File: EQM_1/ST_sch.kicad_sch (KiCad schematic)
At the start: 45 parts, among them J302 Screw_Terminal_01x05, U301 LM35-D, U302 TL082, U303 TL082, U304 LM4040DEX3-2.5+T, U305 TL082

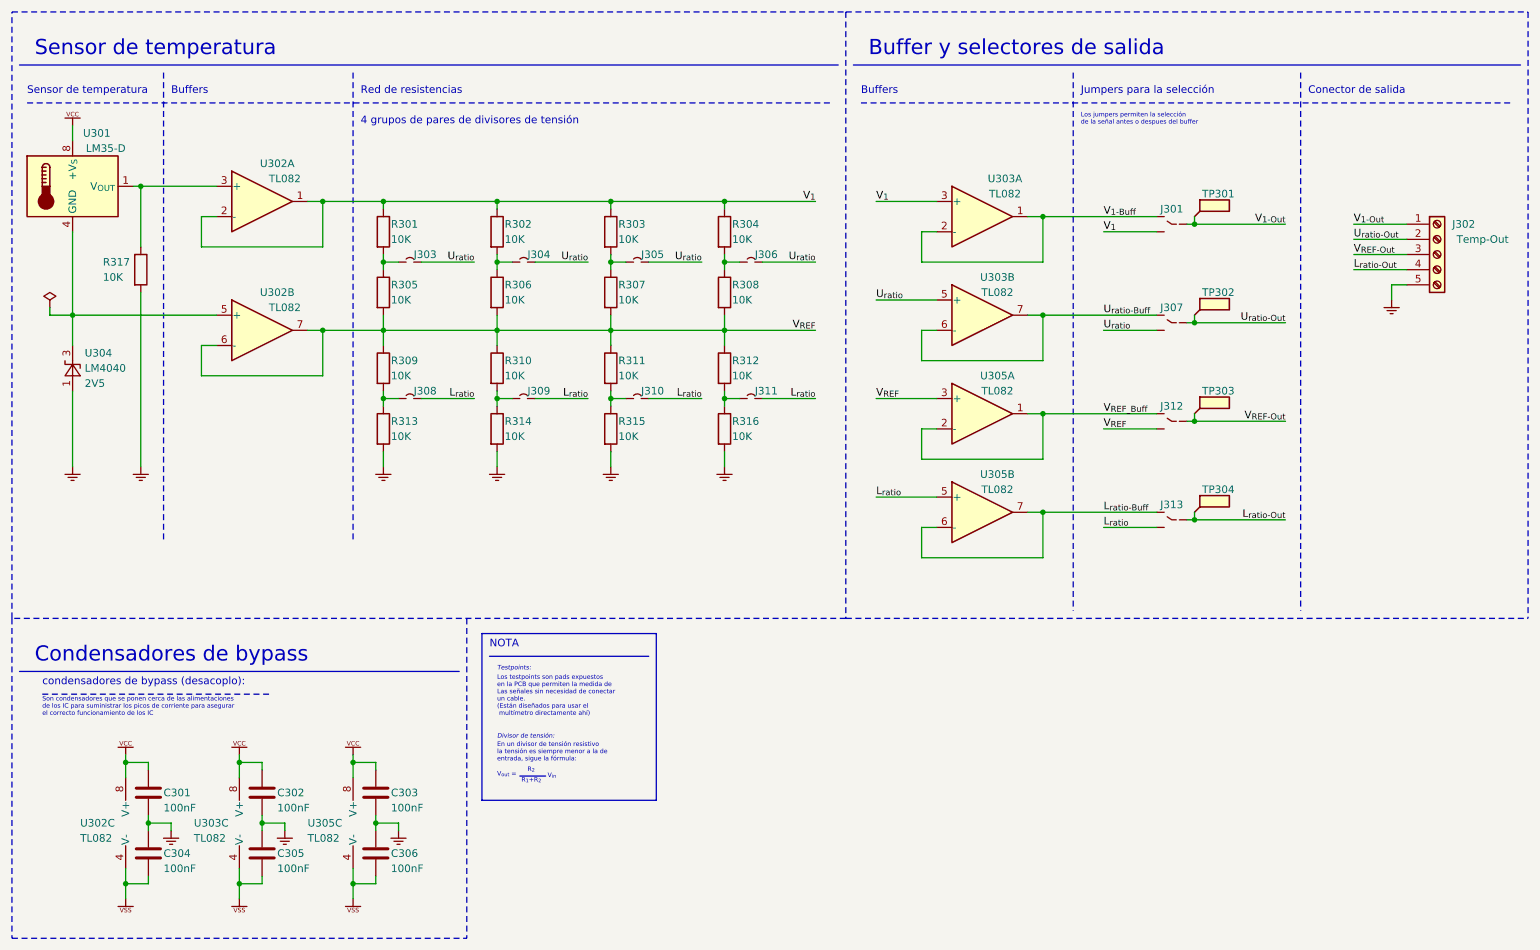
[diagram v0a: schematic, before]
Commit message: Esquema finalizado
El esquema está finalizado a falta de la asociación de footprints y la selección de valores para los pasivos
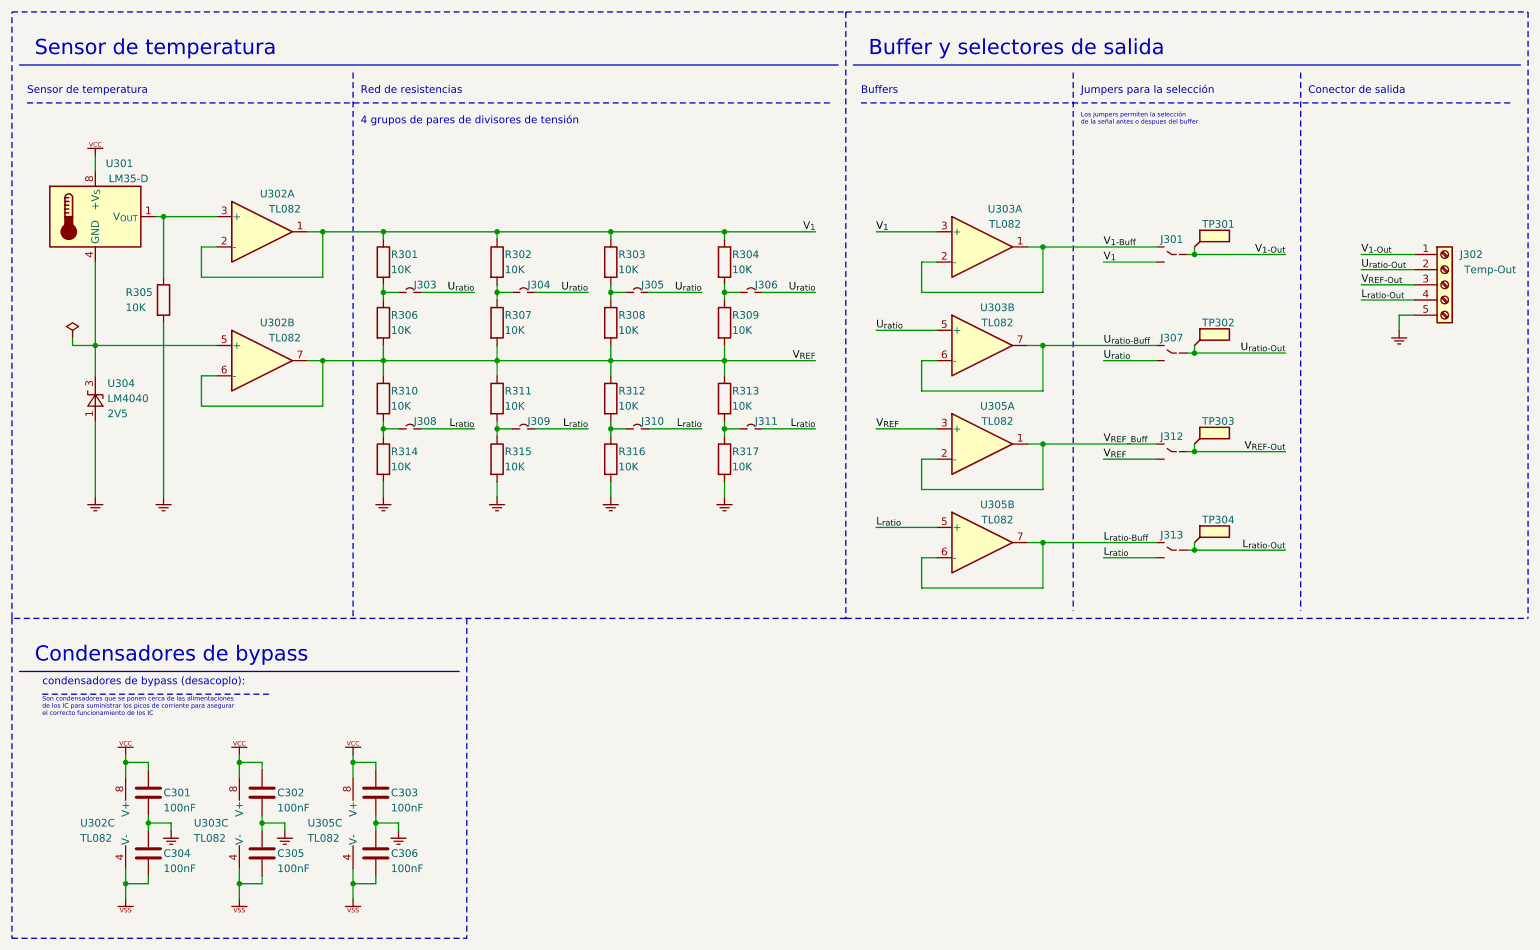
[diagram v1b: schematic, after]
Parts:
- renumbered R317 to R305, R305 to R306, R306 to R307, R307 to R308, R308 to R309, R309 to R310, R310 to R311, R311 to R312, R312 to R313, R313 to R314, R314 to R315, R315 to R316, R316 to R317
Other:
- note removed: "Divisor de tensión:"
- note removed: "En un divisor de tensión resistivo la tensión es siempre menor a la de entrada, sigue la fórmula:"
- note removed: "Los testpoints son pads expuestos en la PCB que permiten la medida de Las señales sin necesidad de conectar un cable. (Están diseñados para usar el multímetro directamente ahí)"
- note removed: "NOTA"
- note removed: "R_{1}+R_{2}"
- note removed: "R_{2}"
- note removed: "Testpoints:"
- note removed: "V_{in}"
- note removed: "V_{out} ="
- moved on the sheet: J301, J302, J303, J304, J305, J306, J307, J308, J309, J310, J311, J312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

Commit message: PCB-1
Primer posicionamiento de los componentes en la pcb y ligeros cambios en el esquemático.
Posicionamiento MUY BASTO, simplemente para ver que los componentes caben en las dimensiones de la pcb elegida.
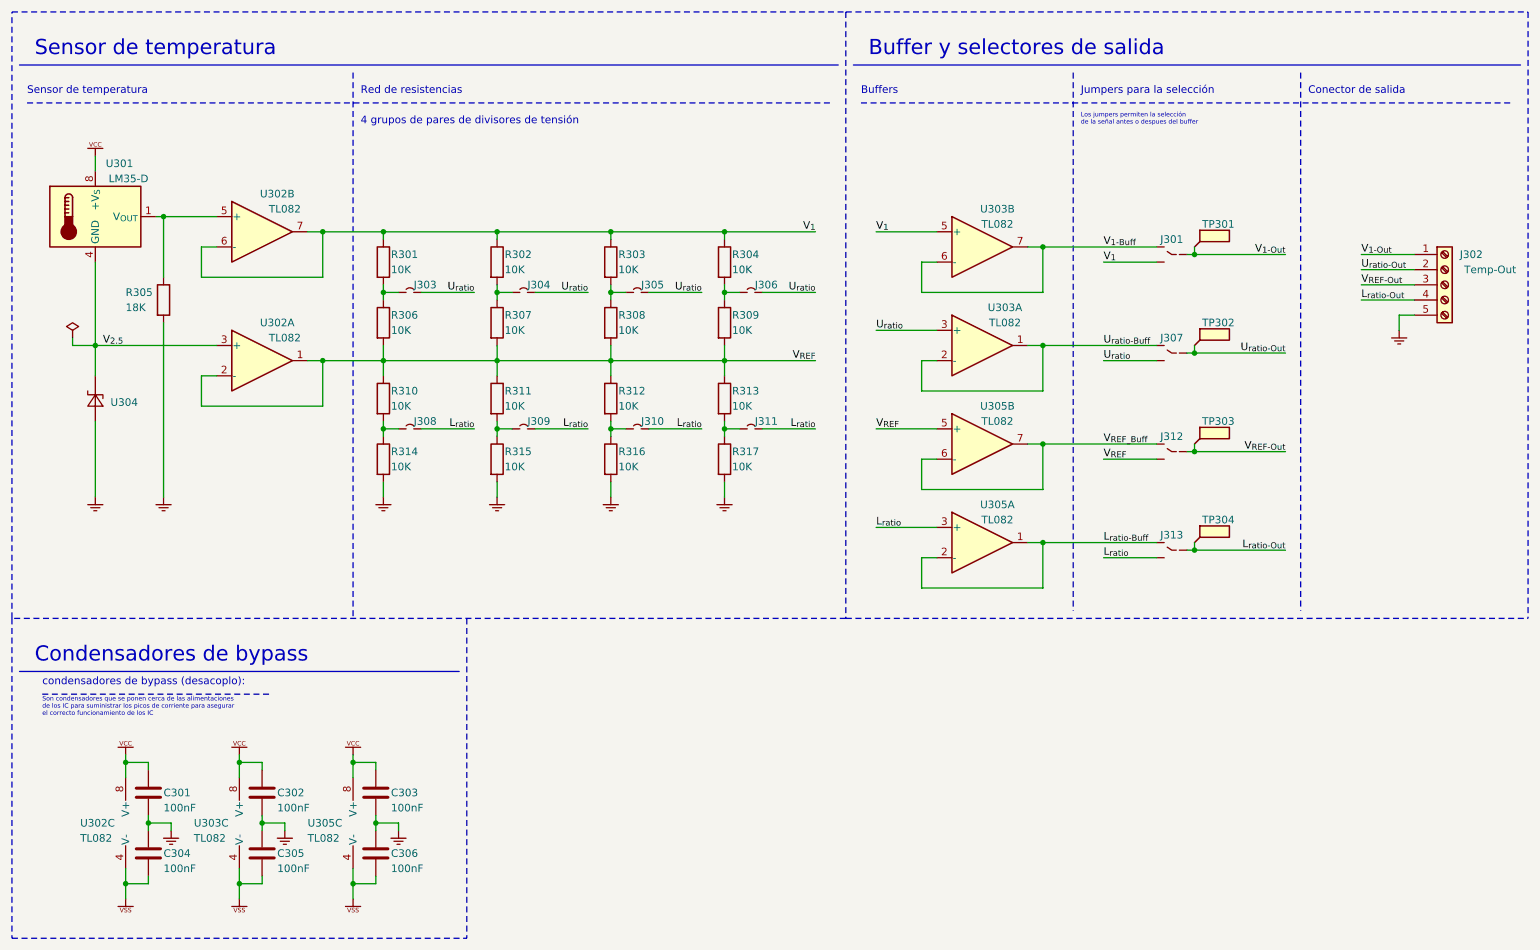
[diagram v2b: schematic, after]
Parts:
- removed U304: LM4040DEX3-2.5+T, Package_TO_SOT_SMD:SOT-353_SC-70-5, symbol Reference_Voltage:LM4040DCK-2.5
- added U304: ~, Package_TO_SOT_SMD:SOT-323_SC-70, symbol Cmisc:LM4040-2.5
- C301, C302, C303, C304, C305, C306: footprint (none) -> Capacitor_SMD:C_0805_2012Metric_Pad1.18x1.45mm_HandSolder
- J301, J307, J312, J313: footprint (none) -> Connector_PinHeader_2.54mm:PinHeader_1x03_P2.54mm_Vertical
- J302: footprint (none) -> TerminalBlock_Phoenix:TerminalBlock_Phoenix_MKDS-1,5-5-5.08_1x05_P5.08mm_Horizontal
- J303, J304, J305, J306, J308, J309, J310, J311: footprint (none) -> Connector_PinHeader_2.54mm:PinHeader_1x02_P2.54mm_Vertical
- R301, R302, R303, R306, R307, R308, R310, R311, R312, R314, R315, R316: footprint (none) -> Resistor_SMD:R_0805_2012Metric_Pad1.20x1.40mm_HandSolder
- R304, R309, R313, R317: footprint (none) -> Resistor_THT:R_Axial_DIN0207_L6.3mm_D2.5mm_P7.62mm_Horizontal
- R305: value 10K -> 18K; footprint (none) -> Resistor_SMD:R_0805_2012Metric_Pad1.20x1.40mm_HandSolder
- TP301, TP302, TP303, TP304: footprint (none) -> TestPoint:TestPoint_Pad_2.0x2.0mm
- U302, U303, U305: footprint (none) -> Package_TO_SOT_SMD:SOT-23-8
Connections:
- net GND: now also U304.1 (A)
- net L_{ratio-Buff}: now also J313.1, U305.1, U305.2 (-); no longer J313.2, U305.6 (-), U305.7
- net L_{ratio-Out}: now also J313.2; no longer J313.1
- net L_{ratio}: now also U305.3 (+); no longer U305.5 (+)
- net U_{ratio-Buff}: now also J307.1, U303.1, U303.2 (-); no longer J307.2, U303.6 (-), U303.7
- net U_{ratio-Out}: now also J307.2; no longer J307.1
- net U_{ratio}: now also U303.3 (+); no longer U303.5 (+)
- net V_{1-Buff}: now also J301.1, U303.6 (-), U303.7; no longer J301.2, U303.1, U303.2 (-)
- net V_{1-Out}: now also J301.2; no longer J301.1
- net V_{1}: now also U302.6 (-), U302.7, U303.5 (+); no longer U302.1, U302.2 (-), U303.3 (+)
- net V_{REF-Out}: now also J312.2; no longer J312.1
- net V_{REF_Buff}: now also J312.1, U305.6 (-), U305.7; no longer J312.2, U305.1, U305.2 (-)
- net V_{REF}: now also U302.1, U302.2 (-), U305.5 (+); no longer U302.6 (-), U302.7, U305.3 (+)
- net at U302.5 (+): now also R305.1, U301.1 (V_{OUT}); no longer U301.4 (GND)
- net #VSS renamed VSS
- new net V_{2.5}: U301.4 (GND), U302.3 (+), U304.2 (K)
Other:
- moved on the sheet: U302A, U302B, U303A, U303B, U305A, U305B
